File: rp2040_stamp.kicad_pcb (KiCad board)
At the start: 4 copper layers, 25 x 25 mm, 75 parts, among them J1 Conn_South, J2 Conn_North, J3 Conn_East, J4 Conn_West, Q1 BSS84, SW1 SW_RESET, U1 RP2040, U2 AP2112K-3.3, U3 W25Q64JV, U4 MCP73831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

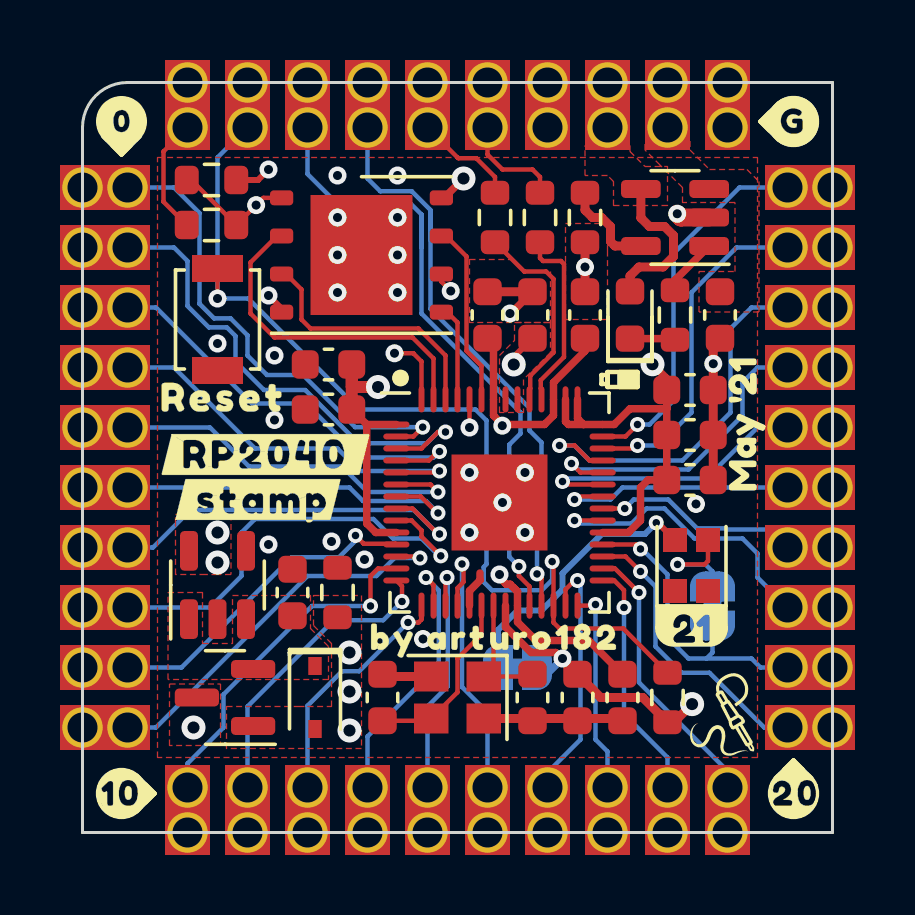
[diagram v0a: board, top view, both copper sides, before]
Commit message: simplify stamp
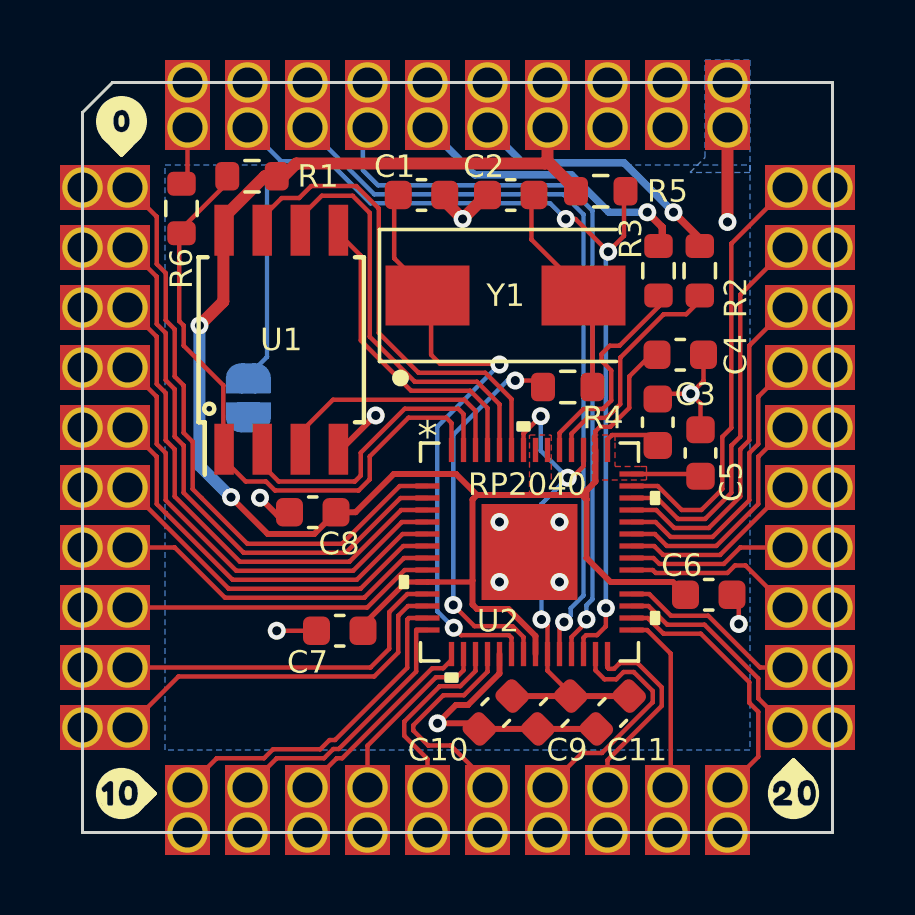
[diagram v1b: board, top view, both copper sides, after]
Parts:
- removed the ? at (144.8, 106.9)
- removed the ? at (160.0, 107.7)
- removed the ? at (143.7, 103.5)
- removed the ? at (152.8, 111.5)
- removed the ? at (162.7, 94.3)
- removed the ? at (145.1, 105.4)
- removed the ? at (160.0, 112.7)
- removed C12: 0.1uF, Capacitor_SMD:C_0603_1608Metric
- removed C13: 1uF, Capacitor_SMD:C_0603_1608Metric
- removed C14, C15: 12pF, Capacitor_SMD:C_0603_1608Metric
- removed C16: 10uF, Capacitor_SMD:C_0603_1608Metric
- removed D1: D_Schottky_Small, Diode_SMD:D_SOD-323
- removed D2: LED_CHR, LED_SMD:LED_0603_1608Metric
- removed D3: WS2812B-2020, LED_SMD_Extra:WS2812B-2020
- removed G***: LOGO, Symbols_Extra:SolderParty-New-Logo_3x2.5mm_SilkScreen
- removed G***: LOGO, LOGO
- removed G***: LOGO, Symbols_Extra:SolderParty-New-Logo_5x4.2mm_SilkScreen
- removed JP1: Jumper_Neopixel_VDD, Jumper:SolderJumper-2_P1.3mm_Bridged_RoundedPad1.0x1.5mm
- removed JP2: Jumper_Neopixel, Jumper:SolderJumper-2_P1.3mm_Bridged_RoundedPad1.0x1.5mm
- removed Q1: BSS84, Package_TO_SOT_SMD:SOT-23
- removed R7: 2K, Resistor_SMD:R_0603_1608Metric
- removed R8: 1K, Resistor_SMD:R_0603_1608Metric
- removed U3: W25Q64JV, Package_SON:WSON-8-1EP_6x5mm_P1.27mm_EP3.4x4mm
- removed U4: MCP73831, Package_TO_SOT_SMD:SOT-23-5
- removed the svg2mod at (161.2, 104.4)
- removed the svg2mod at (156.5, 96.4)
- removed the svg2mod at (142.7, 106.5)
- removed the svg2mod at (150.9, 113.1)
- removed the svg2mod at (159.3, 111.2)
- removed the svg2mod at (158.5, 97.4)
- removed the svg2mod at (150.3, 112.0)
- added C2: 27pF, Capacitor_SMD:C_0603_1608Metric, F.Cu at (153.3, 96.8)
- added C9: 0.1uF, Capacitor_SMD:C_0603_1608Metric, F.Cu at (154.7, 114.0)
- C1: value 0.1uF -> 27pF
- C10: value 1uF -> 0.1uF
- C11, C8: value 0.1uF -> 1uF
- C6, C7: value 10uF -> 0.1uF
- R1: value 1K -> 10K
- R2: value 10K -> 27R
- R4: value 27R -> 1k
- R6: value 100K -> 1K
- SW1: footprint Button_Switch_SMD:SW_SPST_B3U-1000P -> Jumper:SolderJumper-2_P1.3mm_Open_RoundedPad1.0x1.5mm; moved to B.Cu
- U1: value RP2040 -> W25Q64JV; footprint Package_DFN_QFN_Extra:QFN-56_EP_7x7_Pitch0.4mm -> Package_SO:SOIC-8W_5.3x5.3mm_P1.27mm
- U2: value AP2112K-3.3 -> RP2040; footprint Package_TO_SOT_SMD:SOT-23-5 -> UserLib:RP2040
- Y1: value XYDBPCNANF-12MHZ -> Crystal; footprint Crystal:Crystal_SMD_2520-4Pin_2.5x2.0mm -> UserLib:Crystal_SMD_7040-2Pin_7.0x4.0mm
- moved R2 14.3 mm to (159.6, 99.3)
- moved C6 13.9 mm to (159.9, 110.1), turned to 0 degrees
- moved R6 13.8 mm to (142.3, 97.2)
- moved Y1 13.5 mm to (153.1, 100.1), turned to 0 degrees
- moved R5 13.0 mm to (156.3, 96.6)
- moved C10 12.5 mm to (152.8, 114.0), turned to -135 degrees
- moved U2 10.5 mm to (153.9, 108.7), turned to 0 degrees
- moved C8 9.84 mm to (146.7, 107.3), turned to 180 degrees
- moved C3 9.56 mm to (158.2, 104.3), turned to 90 degrees
- moved U1 9.08 mm to (145.6, 101.6), turned to 90 degrees
- moved C7 7.38 mm to (147.6, 111.3), turned to 180 degrees
- moved C1 6.44 mm to (150.3, 96.8), turned to 0 degrees
- moved R4 6.15 mm to (155.2, 103.2), turned to 180 degrees
- moved R3 4.33 mm to (158.2, 99.3)
- moved C4 4.19 mm to (158.9, 102.1)
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- renumbered J4 to J1, J1 to J3, J3 to J4
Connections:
- C1 pad 1: +3V3 -> Net-(C1-Pad1)
- C10 pad 1: +3V3 -> Net-(C10-Pad1)
- C11 pad 1: Net-(C11-Pad1) -> Net-(C10-Pad1)
- C6 pad 1: /VIN -> +3V3
- C7 pad 1: GND -> +3V3
- C7 pad 2: +3V3 -> GND
- R1 pad 1: /USBBOOT -> /~{QSPI_CS}
- R1 pad 2: /~{QSPI_CS} -> +3V3
- R2 pad 1: +3V3 -> /D-
- R2 pad 2: /~{RESET} -> /USB_D-
- R3 pad 1: /D- -> /D+
- R3 pad 2: /USB_D- -> /USB_D+
- R4 pad 1: /D+ -> Net-(C2-Pad1)
- R4 pad 2: /USB_D+ -> Net-(R4-Pad2)
- R5 pad 1: /~{QSPI_CS} -> +3V3
- R5 pad 2: +3V3 -> /~{RESET}
- R6 pad 1: GND -> /USBBOOT
- R6 pad 2: +5V -> /~{QSPI_CS}
- U1 pad 1: +3V3 -> /~{QSPI_CS}
- U1 pad 2: /GPIO0 -> /QSPI_SD1
- U1 pad 3: /GPIO1 -> /QSPI_SD2
- U1 pad 4: /GPIO2 -> GND
- U1 pad 5: /GPIO3 -> /QSPI_SD0
- U1 pad 6: /GPIO4 -> /QSPI_SCLK
- U1 pad 7: /GPIO5 -> /QSPI_SD3
- U1 pad 8: /GPIO6 -> +3V3
- U2 pad 1: /VIN -> +3V3
- U2 pad 2: GND -> /GPIO0
- U2 pad 3: /VIN -> /GPIO1
- U2 pad 4: unconnected-(U2-Pad4) -> /GPIO2
- U2 pad 5: +3V3 -> /GPIO3
- Y1 pad 1: Net-(C15-Pad1) -> Net-(C1-Pad1)
- Y1 pad 2: GND -> Net-(C2-Pad1)
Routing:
- net +5V: track 43.0 -> 0.00 mm, vias 3 -> 0
- net VBAT: track 40.0 -> 0.00 mm, vias 1 -> 0
- net +3V3: track 35.7 -> 65.0 mm, vias 9 -> 2
- net Net-(C1-Pad1): track 0.00 -> 20.9 mm, vias 0 -> 2
- net Net-(C11-Pad1): track 19.7 -> 0.00 mm, vias 2 -> 0
- net Net-(C10-Pad1): track 0.00 -> 16.9 mm, vias 0 -> 3
- net Net-(R4-Pad2): track 0.00 -> 12.5 mm, vias 0 -> 2
- net /QSPI_SD3: track 6.09 -> 15.8 mm
- net Net-(D3-Pad4): track 8.68 -> 0.00 mm, vias 1 -> 0
- net /QSPI_SCLK: track 6.44 -> 13.8 mm, vias 2 -> 0
- net Net-(C2-Pad1): track 0.00 -> 7.21 mm
- net /QSPI_SD0: track 3.24 -> 10.4 mm
- net /USB_D+: track 3.46 -> 9.83 mm, vias 0 -> 1
- net /~{QSPI_CS}: track 14.3 -> 20.5 mm, vias 2 -> 0
- net Net-(C14-Pad1): track 6.11 -> 0.00 mm
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- added copper zone on B.Cu, net GND
- removed copper zone on In2.Cu, net +3V3
- removed copper zone on F.Cu, net +5V
- removed copper zone on F.Cu, net /VIN
- removed copper zone on F.Cu, net GND
- removed copper zone on In1.Cu, net GND
- removed copper zone on F.Cu, net VBAT
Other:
- outline, holes or cut-outs redrawn
- copper layers 4 -> 2
- board text removed: "12MHz"
- board text removed: "AP 2112K"
- board text removed: "Diode"
- board text removed: "MCP 73831"
